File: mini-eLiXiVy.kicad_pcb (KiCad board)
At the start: 2 copper layers, 302.2 x 93.5 mm, 175 parts, among them J1 TYPE-C-31-M12_13_EDITED, J2 AVR-ISP-6, SW1 SW_Push, U1 ATmega32U4-AU, U2 WE-TVS-82400102, Y1 Crystal_GND24_Small

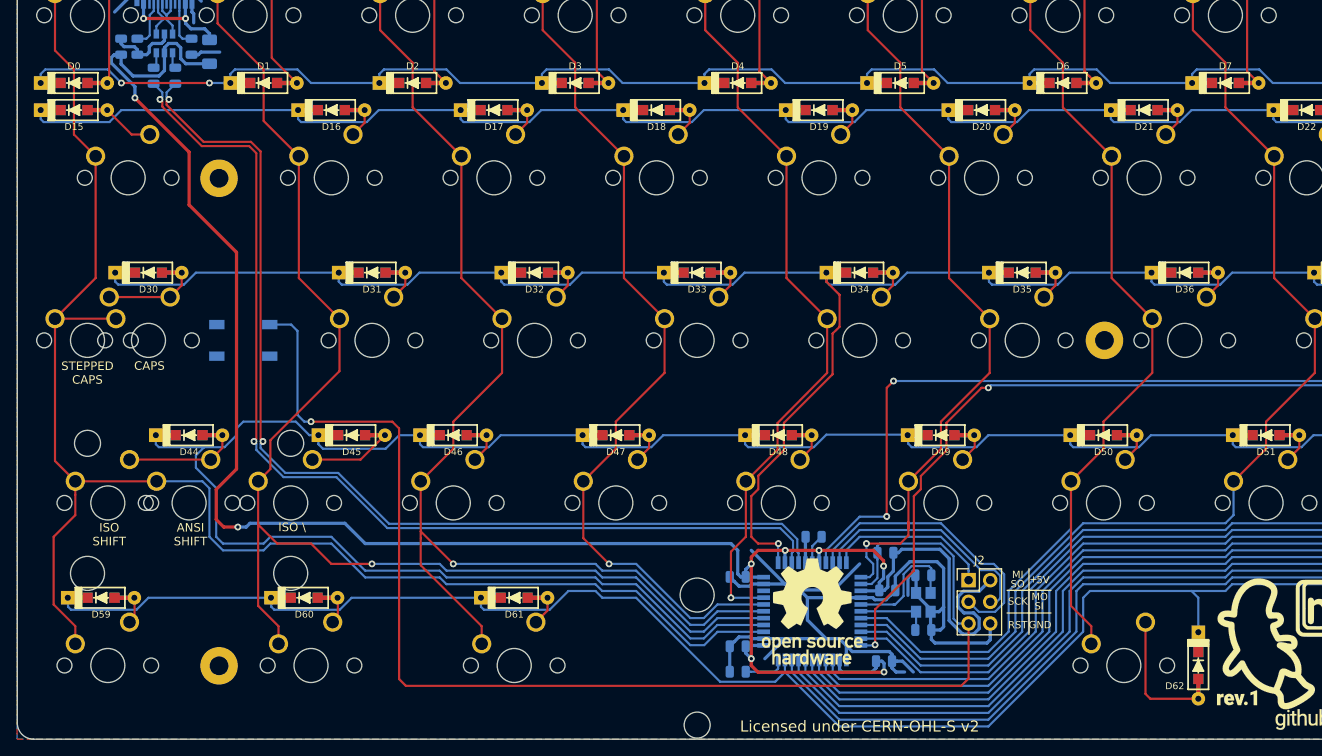
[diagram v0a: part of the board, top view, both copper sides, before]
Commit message: Changed R2/R3 location, redid D+/D- traces.
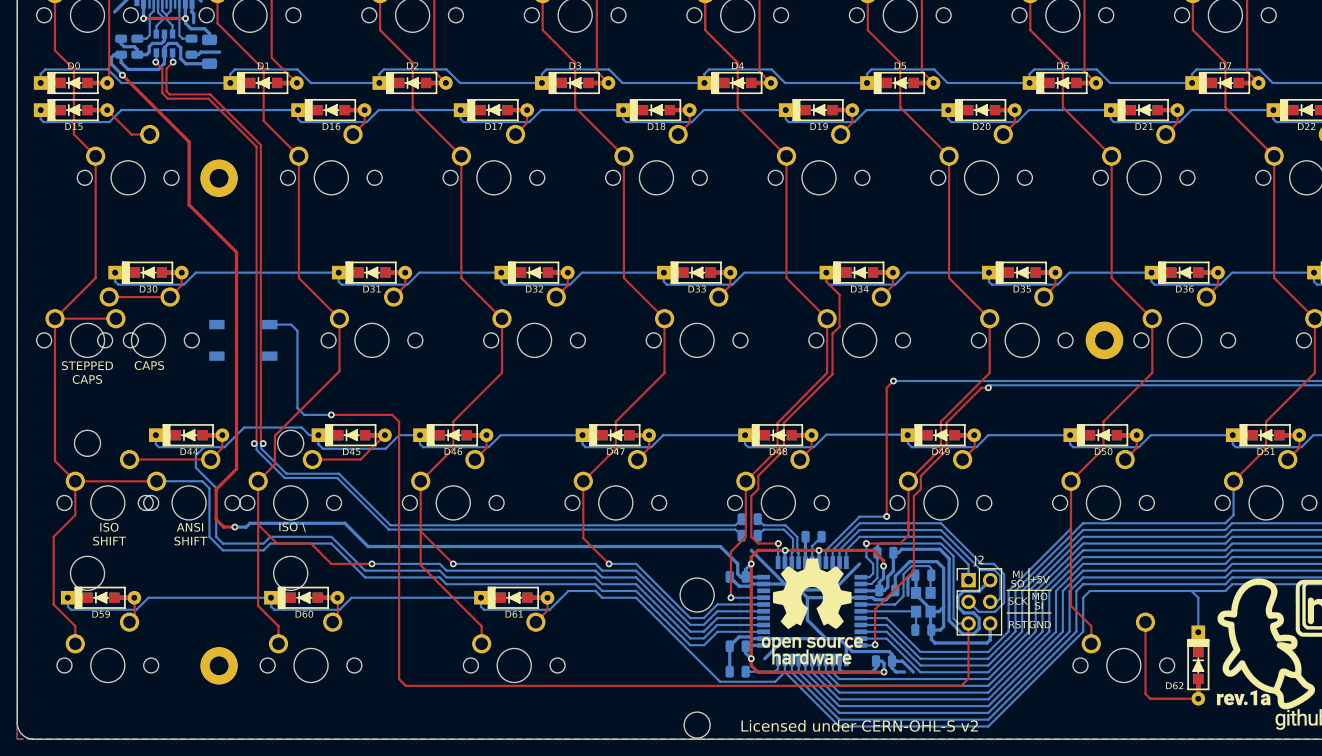
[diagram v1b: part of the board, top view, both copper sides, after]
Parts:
- LO0: footprint mini-Logos:eLiXiVy-SilkScreen-rev1 -> mini-Logos:eLiXiVy-SilkScreenv2
- moved R3 88.2 mm to (99.8, 85.6), turned to 180 degrees
- moved R2 85.0 mm to (99.8, 83.7), turned to 180 degrees
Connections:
- net Net-(R2-Pad1) renamed D+
- net Net-(R3-Pad1) renamed D-
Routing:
- net D-: track 121.5 -> 7.75 mm, vias 2 -> 0
- net MCU_D-: track 1.91 -> 115.5 mm, vias 0 -> 2
- net D+: track 121.5 -> 8.58 mm, vias 2 -> 0
- net MCU_D+: track 1.91 -> 114.7 mm, vias 0 -> 2
- net +5V: track 250.6 -> 248.5 mm
- net ROW3: track 380.1 -> 379.1 mm
- net ROW0: vias 3 -> 1

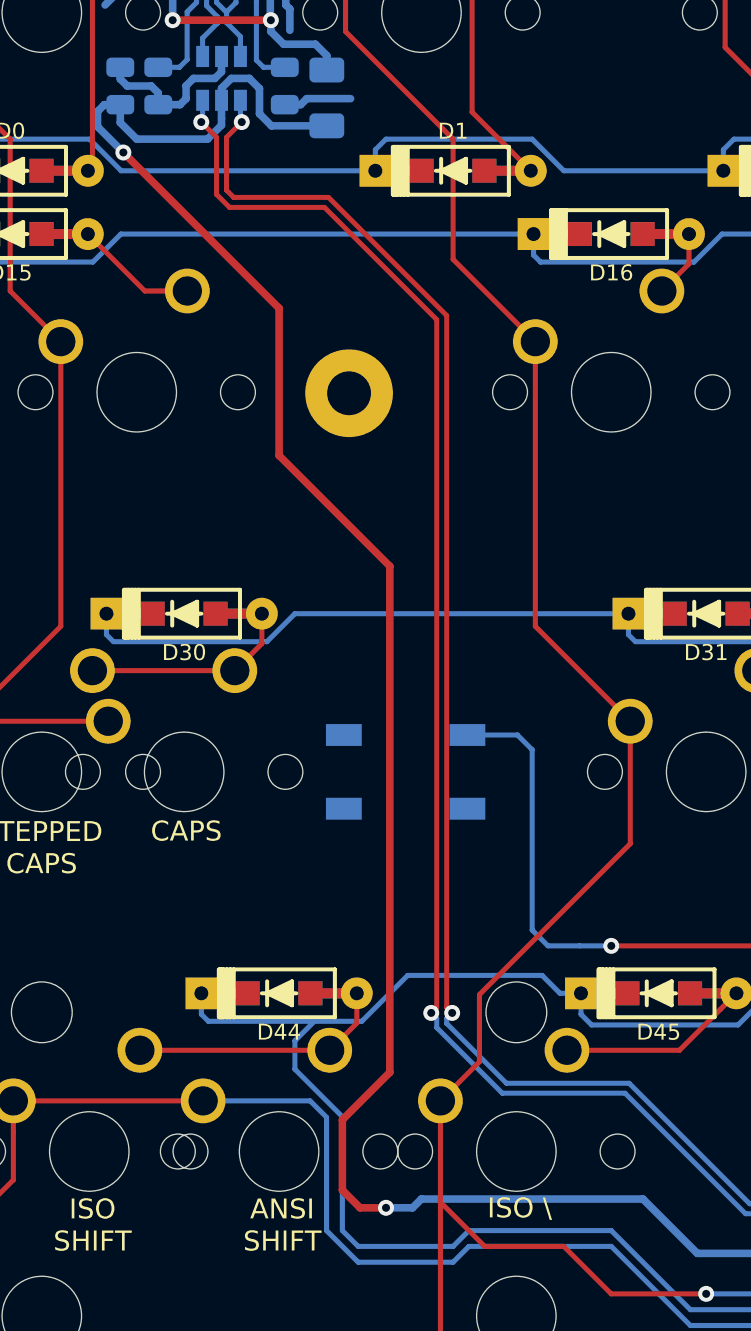
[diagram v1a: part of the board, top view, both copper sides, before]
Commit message: Reran +5V and data lines
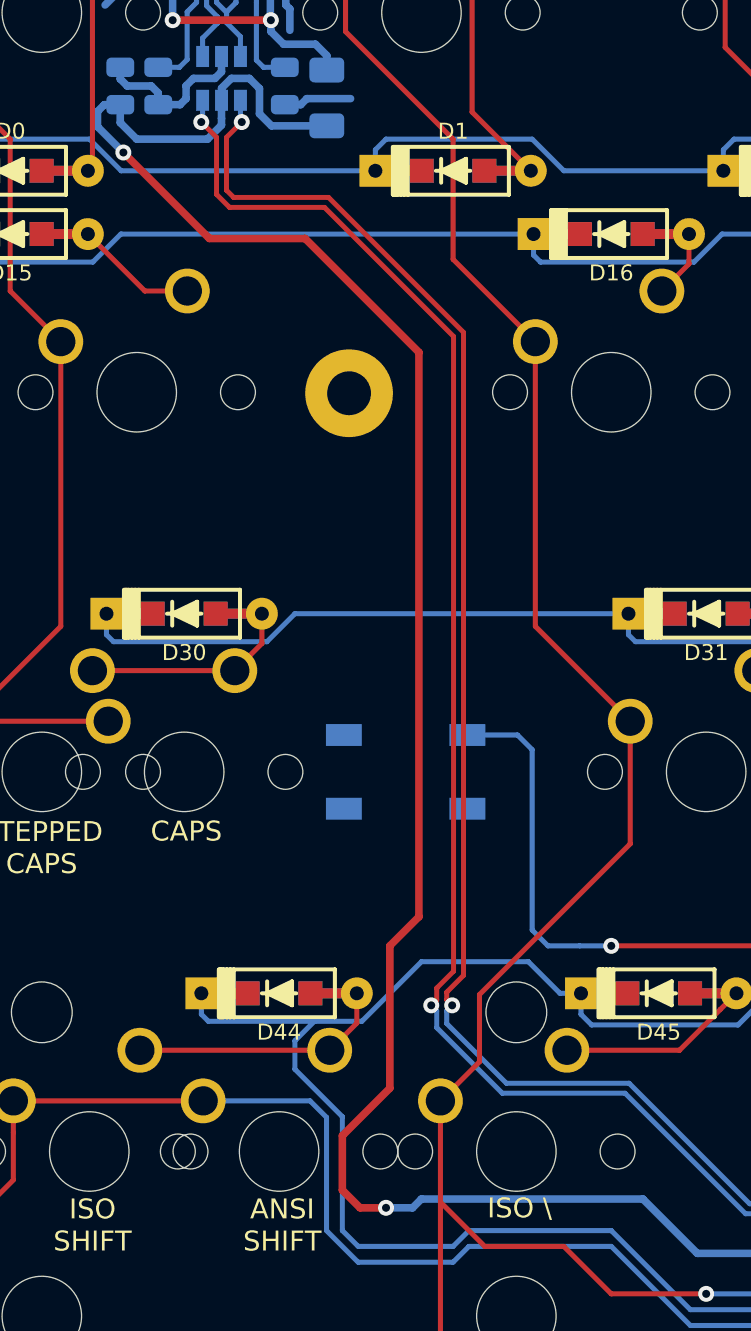
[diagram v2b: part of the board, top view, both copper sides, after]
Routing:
- net +5V: track 248.5 -> 252.5 mm
- net MCU_D+: track 114.7 -> 115.4 mm
- net MCU_D-: track 115.5 -> 116.2 mm
- net ROW3: track 379.1 -> 379.7 mm

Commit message: Moved R2, R3 and rerouted data line/rotary encoder traces
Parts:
- moved R1 2.64 mm to (118.4, 87.4)
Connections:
- net REA renamed RE-
- net REB renamed RE+
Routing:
- net RE+: track 252.3 -> 283.8 mm
- net COL14: track 302.0 -> 282.9 mm
- net RE-: track 247.0 -> 265.1 mm
- net +5V: track 252.5 -> 250.1 mm
- net COL5: track 84.9 -> 83.2 mm
- net RESET: track 154.2 -> 153.1 mm
- net ROW0_RE: track 21.5 -> 22.5 mm

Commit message: Updated logo, refined data line traces.
Logos have been updated to match the revision number, rev.1.1
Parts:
- LO0: footprint mini-Logos:eLiXiVy-SilkScreenv2 -> mini-Logos:eLiXiVy-rev1.1-SilkScreen
- LO1: footprint mini-Logos:eLiXiVy-Maskv2 -> mini-Logos:eLiXiVy-rev1.1-Mask
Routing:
- net COL14: track 282.9 -> 306.1 mm
- net RESET: track 153.1 -> 145.4 mm
- net COL8: track 145.4 -> 142.6 mm
- net COL12: track 267.9 -> 265.1 mm
- net COL11: track 235.4 -> 232.6 mm
- net COL7: track 126.1 -> 123.3 mm
- net COL9: track 194.0 -> 191.2 mm
- net COL10: track 222.3 -> 219.5 mm
- net ROW1: track 566.7 -> 563.9 mm
- net ROW0: track 566.0 -> 563.2 mm
- net COL13: track 287.9 -> 285.1 mm
- net ROW4: track 321.4 -> 319.1 mm
- net COL3: track 99.3 -> 100.7 mm
- net ROW0_RE: track 22.5 -> 21.3 mm
- net COL2: track 134.4 -> 133.4 mm
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
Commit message: Refined data line, rotary encoder and +5V traces
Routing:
- net ROW2: track 341.3 -> 357.8 mm
- net ROW0_RE: track 21.3 -> 28.6 mm
- net COL14: track 306.1 -> 299.7 mm
- net ROW3: track 379.7 -> 382.5 mm
- net COL0: track 183.6 -> 182.3 mm
- net RE+: track 283.9 -> 282.9 mm
- net +5V: track 250.1 -> 250.7 mm
- net RE-: track 265.1 -> 264.5 mm

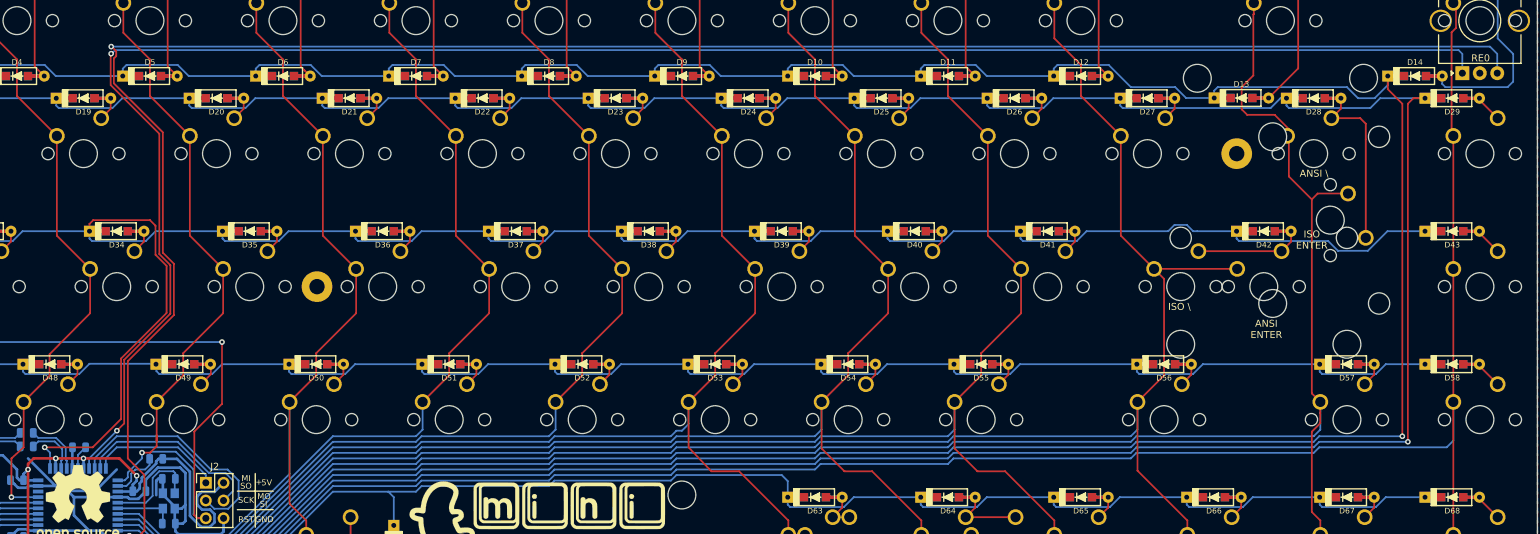
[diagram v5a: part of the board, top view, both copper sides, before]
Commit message: Redid the rotary encoder traces
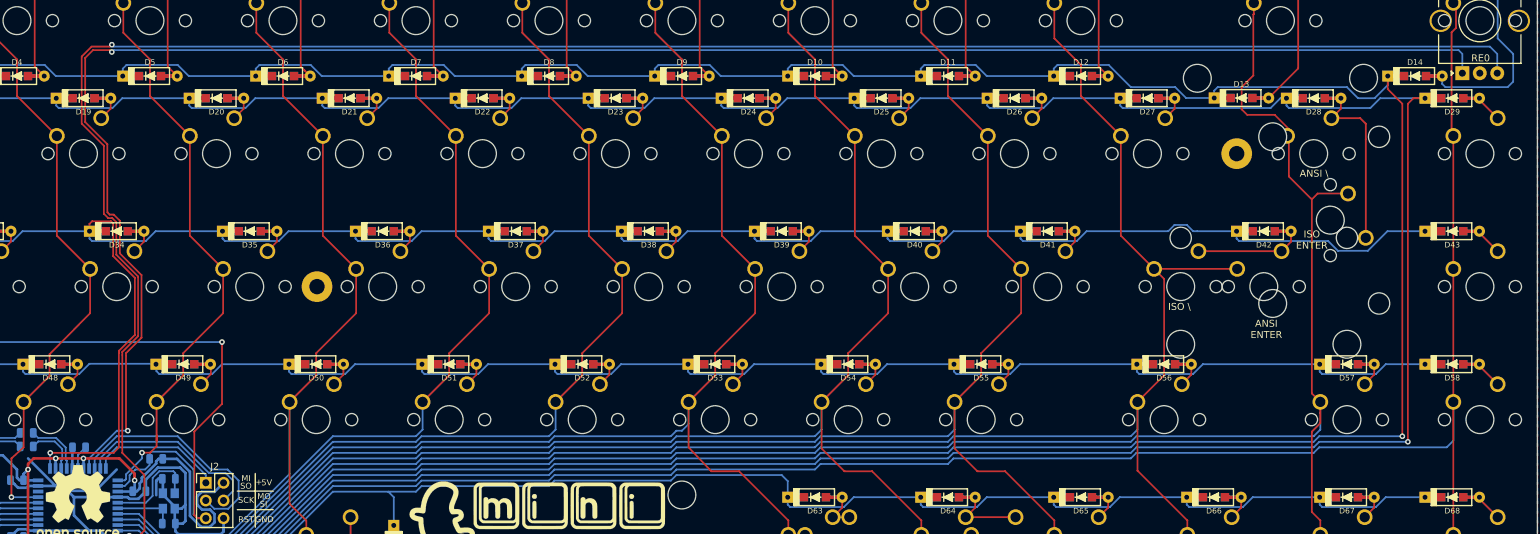
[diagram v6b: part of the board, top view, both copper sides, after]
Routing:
- net ROW2: track 357.8 -> 351.2 mm
- net RE-: track 264.5 -> 267.7 mm
- net RE+: track 282.9 -> 284.8 mm

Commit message: Updated to rev.1.1
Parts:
- moved R1 2.62 mm to (116.1, 88.6)
- moved D13 0.63 mm to (274.4, 35.7)
- moved D28 0.32 mm to (284.5, 35.7)
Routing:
- net COL13: track 285.1 -> 282.9 mm
- net RESET: track 145.2 -> 143.8 mm
- net ROW0_RE: track 28.6 -> 27.6 mm
- net ROW0: track 563.4 -> 562.8 mm
- net COL5: track 82.6 -> 83.3 mm
